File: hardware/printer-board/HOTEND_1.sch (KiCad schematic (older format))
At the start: 7 parts, among them J24 HOT_END, Q3 WSK220N04

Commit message: update,
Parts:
- J24: footprint footprint-lib:s2b-ph-kl,hotend_output -> footprint-lib:mpt_0,5%2f2-2,54,heatbed
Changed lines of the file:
@@
 $Descr A4 11693 8268
 encoding utf-8
-Sheet 28 34
+Sheet 28 33
 Title ""
 Date ""
@@
 F 0 "J24" H 5219 2825 50  0000 C CNN
 F 1 "HOT_END" H 5219 2916 50  0000 C CNN
-F 2 "footprint-lib:s2b-ph-kl,hotend_output" H 5300 3150 50  0001 C CNN
+F 2 "footprint-lib:mpt_0,5%2f2-2,54,heatbed" H 5300 3150 50  0001 C CNN
 F 3 "~" H 5300 3150 50  0001 C CNN
 	1    5300 3150

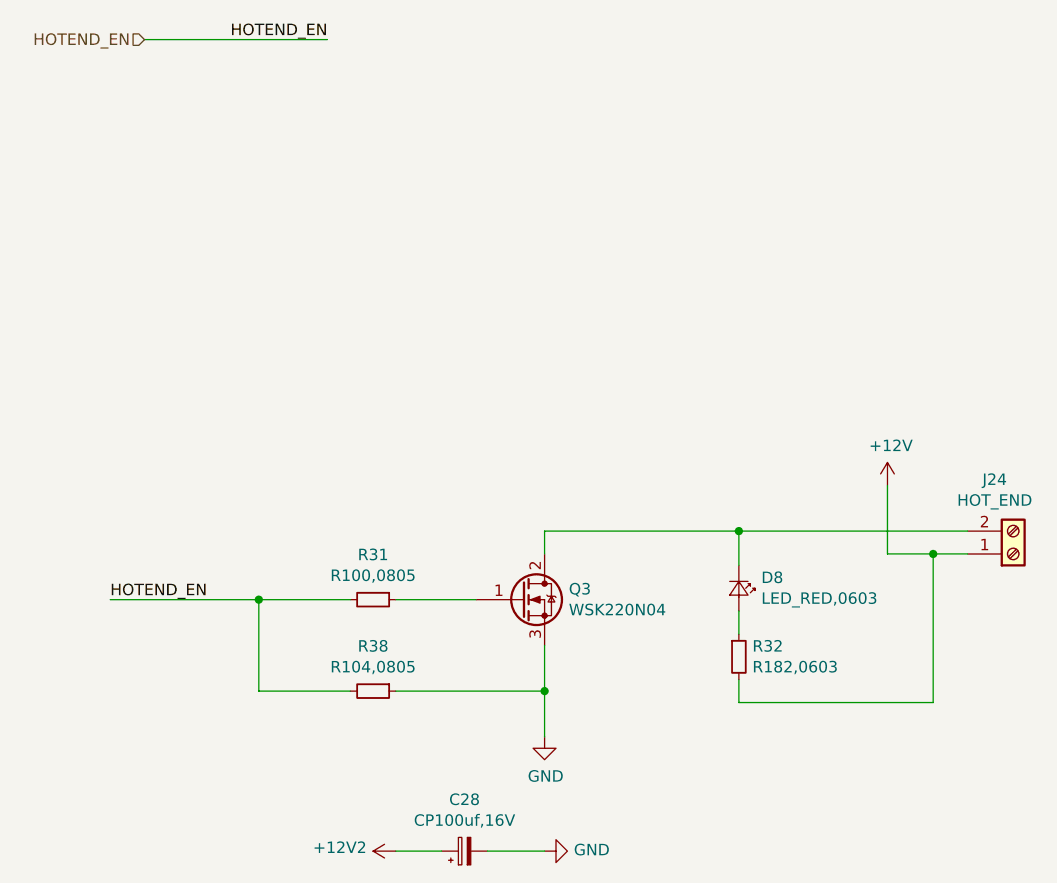
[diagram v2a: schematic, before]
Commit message: update hotend MOSFET,
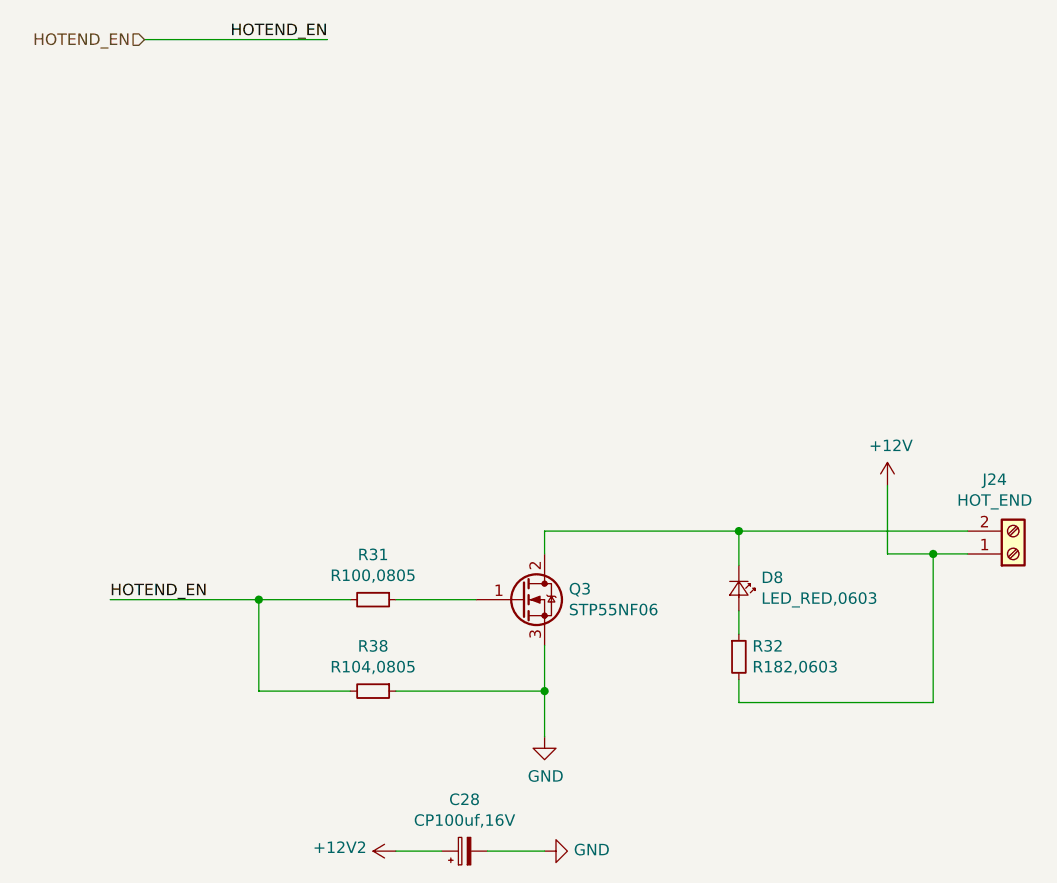
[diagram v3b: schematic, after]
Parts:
- Q3: value WSK220N04 -> STP55NF06
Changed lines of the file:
@@
 $Descr A4 11693 8268
 encoding utf-8
-Sheet 28 32
+Sheet 26 32
 Title ""
 Date ""
@@
 AR Path="/5CC22025/5CC222D3/5CC2240F" Ref="Q3"  Part="1"
 F 0 "Q3" H 3356 3396 50  0000 L CNN
-F 1 "WSK220N04" H 3356 3305 50  0000 L CNN
+F 1 "STP55NF06" H 3356 3305 50  0000 L CNN
 F 2 "Package_TO_SOT_SMD:TO-263-2" H 3350 3450 50  0001 C CNN
 F 3 "~" H 3150 3350 50  0001 C CNN

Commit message: update,
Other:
- moved on the sheet: D8, J24, R32
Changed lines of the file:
@@
 L Connector:Screw_Terminal_01x02 J?
 U 1 1 5CC22399
-P 5300 3150
+P 5300 2950
 AR Path="/5CC0B758/5CC22399" Ref="J?"  Part="1"
 AR Path="/5CC12903/5CC22399" Ref="J?"  Part="1"
 AR Path="/5CC130A8/5CC22399" Ref="J?"  Part="1"
 AR Path="/5CC22025/5CC222D3/5CC22399" Ref="J24"  Part="1"
-F 0 "J24" H 5219 2825 50  0000 C CNN
-F 1 "HOT_END" H 5219 2916 50  0000 C CNN
-F 2 "footprint-lib:mpt_0,5%2f2-2,54,heatbed" H 5300 3150 50  0001 C CNN
-F 3 "~" H 5300 3150 50  0001 C CNN
-	1    5300 3150
-	1    0    0    1
+F 0 "J24" H 5219 2625 50  0000 C CNN
+F 1 "HOT_END" H 5219 2716 50  0000 C CNN
+F 2 "footprint-lib:mpt_0,5%2f2-2,54,heatbed" H 5300 2950 50  0001 C CNN
+F 3 "~" H 5300 2950 50  0001 C CNN
+	1    5300 2950
+	1    0    0    -1
 $EndComp
 $Comp
@@
 L taobao-r:R182,0603 R?
 U 1 1 5CC19EDC
-P 4100 3600
+P 4100 2500
 AR Path="/5CC0B758/5CC19EDC" Ref="R?"  Part="1"
 AR Path="/5CC12903/5CC19EDC" Ref="R?"  Part="1"
 AR Path="/5CC130A8/5CC19EDC" Ref="R?"  Part="1"
 AR Path="/5CC22025/5CC222D3/5CC19EDC" Ref="R32"  Part="1"
-F 0 "R32" H 4159 3646 50  0000 L CNN
-F 1 "R182,0603" H 4159 3555 50  0000 L CNN
-F 2 "Resistor_SMD:R_0603_1608Metric_Pad1.05x0.95mm_HandSolder" H 4100 3600 50  0001 C CNN
-F 3 "~" H 4100 3600 50  0001 C CNN
-	1    4100 3600
-	1    0    0    -1
+F 0 "R32" H 4159 2546 50  0000 L CNN
+F 1 "R182,0603" H 4159 2455 50  0000 L CNN
+F 2 "Resistor_SMD:R_0603_1608Metric_Pad1.05x0.95mm_HandSolder" H 4100 2500 50  0001 C CNN
+F 3 "~" H 4100 2500 50  0001 C CNN
+	1    4100 2500
+	1    0    0    1
 $EndComp
 $Comp
 L taobao-led:LED_RED,0603 D?
 U 1 1 5CC2239F
-P 4100 3300
+P 4100 2800
 AR Path="/5CC0B758/5CC2239F" Ref="D?"  Part="1"
 AR Path="/5CC12903/5CC2239F" Ref="D?"  Part="1"
 AR Path="/5CC130A8/5CC2239F" Ref="D?"  Part="1"
 AR Path="/5CC22025/5CC222D3/5CC2239F" Ref="D8"  Part="1"
-F 0 "D8" V 4054 3398 50  0000 L CNN
-F 1 "LED_RED,0603" V 4145 3398 50  0000 L CNN
-F 2 "LED_SMD:LED_0603_1608Metric_Pad1.05x0.95mm_HandSolder" V 4100 3300 50  0001 C CNN
-F 3 "" V 4100 3300 50  0001 C CNN
-	1    4100 3300
-	0    1    1    0
+F 0 "D8" V 4054 2898 50  0000 L CNN
+F 1 "LED_RED,0603" V 4145 2898 50  0000 L CNN
+F 2 "LED_SMD:LED_0603_1608Metric_Pad1.05x0.95mm_HandSolder" V 4100 2800 50  0001 C CNN
+F 3 "" V 4100 2800 50  0001 C CNN
+	1    4100 2800
+	0    1    -1   0
 $EndComp
 Wire Wire Line
@@
 	3250 3050 3250 3150
 Wire Wire Line
-	4100 3200 4100 3050
+	4100 2900 4100 3050
 Connection ~ 4100 3050
 Wire Wire Line
 	4100 3050 3250 3050
 Wire Wire Line
-	4100 3400 4100 3500
+	4100 2700 4100 2600
 Wire Wire Line
-	5100 3150 4950 3150
+	5100 2950 4950 2950
 Wire Wire Line
-	4950 3150 4950 3800
+	4950 2950 4950 2300
 Wire Wire Line
-	4950 3800 4100 3800
+	4950 2300 4750 2300
 Wire Wire Line
-	4100 3800 4100 3700
-Connection ~ 4950 3150
+	4100 2300 4100 2400
 Text HLabel 1500 900  0    50   Input ~ 0
 HOTEND_EN
@@
 L power:+12V #PWR0252
 U 1 1 5CC22418
-P 4750 2850
-F 0 "#PWR0252" H 4750 2700 50  0001 C CNN
-F 1 "+12V" H 4765 3023 50  0000 C CNN
-F 2 "" H 4750 2850 50  0001 C CNN
-F 3 "" H 4750 2850 50  0001 C CNN
-	1    4750 2850
-	1    0    0    -1
+P 4750 2150
+F 0 "#PWR0252" H 4750 2000 50  0001 C CNN
+F 1 "+12V" H 4765 2323 50  0000 C CNN
+F 2 "" H 4750 2150 50  0001 C CNN
+F 3 "" H 4750 2150 50  0001 C CNN
+	1    4750 2150
+	-1   0    0    -1
 $EndComp
 Wire Wire Line
-	4750 2850 4750 3150
+	4750 2150 4750 2300
+Connection ~ 4750 2300
 Wire Wire Line
-	4750 3150 4950 3150
+	4750 2300 4100 2300
 $EndSCHEMATC

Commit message: update,
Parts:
- removed C28: CP100uf,16V, Capacitor_SMD:CP_Elec_6.3x5.3, symbol taobao-cp:CP100uf,16V
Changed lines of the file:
@@
 $Descr A4 11693 8268
 encoding utf-8
-Sheet 26 32
+Sheet 24 32
 Title ""
 Date ""
@@
 Wire Wire Line
 	2000 3350 2400 3350
-$Comp
-L taobao-components:+12V2 #PWR?
-U 1 1 5CC19F05
-P 2600 4450
-AR Path="/5CC0B758/5CC19F05" Ref="#PWR?"  Part="1"
-AR Path="/5CC12903/5CC19F05" Ref="#PWR?"  Part="1"
-AR Path="/5CC130A8/5CC19F05" Ref="#PWR?"  Part="1"
-AR Path="/5CC22025/5CC222D3/5CC19F05" Ref="#PWR0235"  Part="1"
-F 0 "#PWR0235" H 2600 4300 50  0001 C CNN
-F 1 "+12V2" V 2615 4578 50  0000 L CNN
-F 2 "" H 2600 4450 50  0001 C CNN
-F 3 "" H 2600 4450 50  0001 C CNN
-	1    2600 4450
-	0    -1   -1   0
-$EndComp
-$Comp
-L power:GND #PWR?
-U 1 1 5CC19F0B
-P 3250 4450
-AR Path="/5CC0B758/5CC19F0B" Ref="#PWR?"  Part="1"
-AR Path="/5CC12903/5CC19F0B" Ref="#PWR?"  Part="1"
-AR Path="/5CC130A8/5CC19F0B" Ref="#PWR?"  Part="1"
-AR Path="/5CC22025/5CC222D3/5CC19F0B" Ref="#PWR0236"  Part="1"
-F 0 "#PWR0236" H 3250 4200 50  0001 C CNN
-F 1 "GND" V 3255 4322 50  0000 R CNN
-F 2 "" H 3250 4450 50  0001 C CNN
-F 3 "" H 3250 4450 50  0001 C CNN
-	1    3250 4450
-	0    -1   -1   0
-$EndComp
-$Comp
-L taobao-cp:CP100uf,16V C28
-U 1 1 5CC19F11
-P 2900 4450
-F 0 "C28" V 3125 4450 50  0000 C CNN
-F 1 "CP100uf,16V" V 3034 4450 50  0000 C CNN
-F 2 "Capacitor_SMD:CP_Elec_6.3x5.3" H 2900 4450 50  0001 C CNN
-F 3 "~" H 2900 4450 50  0001 C CNN
-	1    2900 4450
-	0    -1   -1   0
-$EndComp
-Wire Wire Line
-	2600 4450 2800 4450
-Wire Wire Line
-	3000 4450 3250 4450
 $Bitmap
 Pos 9550 5000

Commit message: update,
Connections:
- net HOTEND_EN renamed EN2
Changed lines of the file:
@@
 	4100 2300 4100 2400
 Text HLabel 1500 900  0    50   Input ~ 0
-HOTEND_EN
+EN2
 Text Label 2300 900  2    50   ~ 0
-HOTEND_EN
+EN2
 Wire Wire Line
 	1500 900  2300 900
 Text Label 1350 3350 0    50   ~ 0
-HOTEND_EN
+EN2
 Wire Wire Line
 	1350 3350 2000 3350

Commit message: update,
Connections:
- net -12V: now reaches D8.1 (K), J24.2 (Pin_2), Q3.2 (D)
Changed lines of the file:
@@
 EESchema Schematic File Version 4
-LIBS:printer-board-cache
 EELAYER 26 0
 EELAYER END
 $Descr A4 11693 8268
 encoding utf-8
-Sheet 24 32
+Sheet 1 1
 Title ""
 Date ""
@@
 Wire Wire Line
 	4750 2300 4100 2300
+Text Label 5100 3050 2    50   ~ 0
+-12V
+Text Label 4250 2300 0    50   ~ 0
+12V_led
 $EndSCHEMATC

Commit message: update hotend,
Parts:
- Q3: footprint Package_TO_SOT_SMD:TO-263-2 -> footprint-lib:TO-263-2,drill_array
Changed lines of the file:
@@
 AR Path="/5CC130A8/5CC22399" Ref="J?"  Part="1"
 AR Path="/5CC22025/5CC222D3/5CC22399" Ref="J24"  Part="1"
+AR Path="/5CC22399" Ref="J24"  Part="1"
 F 0 "J24" H 5219 2625 50  0000 C CNN
 F 1 "HOT_END" H 5219 2716 50  0000 C CNN
@@
 AR Path="/5CC130A8/5CC2240F" Ref="Q?"  Part="1"
 AR Path="/5CC22025/5CC222D3/5CC2240F" Ref="Q3"  Part="1"
+AR Path="/5CC2240F" Ref="Q3"  Part="1"
 F 0 "Q3" H 3356 3396 50  0000 L CNN
 F 1 "STP55NF06" H 3356 3305 50  0000 L CNN
-F 2 "Package_TO_SOT_SMD:TO-263-2" H 3350 3450 50  0001 C CNN
+F 2 "footprint-lib:TO-263-2,drill_array" H 3350 3450 50  0001 C CNN
 F 3 "~" H 3150 3350 50  0001 C CNN
 	1    3150 3350
@@
 AR Path="/5CC130A8/5CC2239B" Ref="R?"  Part="1"
 AR Path="/5CC22025/5CC222D3/5CC2239B" Ref="R31"  Part="1"
+AR Path="/5CC2239B" Ref="R31"  Part="1"
 F 0 "R31" V 2304 3350 50  0000 C CNN
 F 1 "R100,0805" V 2395 3350 50  0000 C CNN
@@
 AR Path="/5CC130A8/5CC2239C" Ref="R?"  Part="1"
 AR Path="/5CC22025/5CC222D3/5CC2239C" Ref="R38"  Part="1"
+AR Path="/5CC2239C" Ref="R38"  Part="1"
 F 0 "R38" V 2304 3750 50  0000 C CNN
 F 1 "R104,0805" V 2395 3750 50  0000 C CNN
@@
 AR Path="/5CC130A8/5CC2239D" Ref="#PWR?"  Part="1"
 AR Path="/5CC22025/5CC222D3/5CC2239D" Ref="#PWR0234"  Part="1"
+AR Path="/5CC2239D" Ref="#PWR0234"  Part="1"
 F 0 "#PWR0234" H 3250 3700 50  0001 C CNN
 F 1 "GND" H 3255 3777 50  0000 C CNN
@@
 AR Path="/5CC130A8/5CC19EDC" Ref="R?"  Part="1"
 AR Path="/5CC22025/5CC222D3/5CC19EDC" Ref="R32"  Part="1"
+AR Path="/5CC19EDC" Ref="R32"  Part="1"
 F 0 "R32" H 4159 2546 50  0000 L CNN
 F 1 "R182,0603" H 4159 2455 50  0000 L CNN
@@
 AR Path="/5CC130A8/5CC2239F" Ref="D?"  Part="1"
 AR Path="/5CC22025/5CC222D3/5CC2239F" Ref="D8"  Part="1"
+AR Path="/5CC2239F" Ref="D8"  Part="1"
 F 0 "D8" V 4054 2898 50  0000 L CNN
 F 1 "LED_RED,0603" V 4145 2898 50  0000 L CNN
